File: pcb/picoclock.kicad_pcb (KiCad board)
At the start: 2 copper layers, 175.8 x 64 mm, 54 parts, among them J1 UART, J10 USB, J2 AUDIO, J3 xx, J4 xx, J5 Power In, J6 USB_C_Receptacle, J7 xx, J8 xx, J9 screen_adapter_connector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

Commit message: update case+pcb
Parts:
- added R10: 10K, Resistor_SMD:R_0603_1608Metric, B.Cu at (138.1, 109.4)
- added R11: 10K, Resistor_SMD:R_0603_1608Metric, B.Cu at (138.1, 113.2)
- added R12: 10K, Resistor_SMD:R_0603_1608Metric, B.Cu at (187.9, 112.7)
- added R13: 10K, Resistor_SMD:R_0603_1608Metric, B.Cu at (188.9, 98.5)
- added R8: 10K, Resistor_SMD:R_0603_1608Metric, B.Cu at (189.1, 82.0)
- added R9: 10K, Resistor_SMD:R_0603_1608Metric, B.Cu at (138.1, 106.4)
- H1, H2, H3, H4: footprint MountingHole:MountingHole_2.5mm -> MountingHole:MountingHole_3mm_Pad
- moved JP2 0.21 mm to (69.2, 103.2)
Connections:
- J4 pad 4: unconnected-(J4-Pin_4-Pad4) -> SDA
- J4 pad 5: unconnected-(J4-Pin_5-Pad5) -> SCL
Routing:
- net +3.3V: track 193.4 -> 244.2 mm
- net SDA: track 22.9 -> 72.5 mm, vias 2 -> 3
- net SCL: track 25.4 -> 74.4 mm, vias 0 -> 2
- net GPIO8: track 42.9 -> 45.3 mm
- net GPIO9: track 37.5 -> 39.5 mm

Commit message: [pcb] update
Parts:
- added BT1: 3V Cell, cell:MPD_BC501SM-TR, F.Cu at (214.9, 105.7)
- added J11: Alt Power, Connector_PinHeader_2.54mm:PinHeader_1x02_P2.54mm_Vertical, F.Cu at (171.1, 119.6)
- C1, C2, C3, C4, C5, C9: footprint Capacitor_SMD:C_0402_1005Metric -> Capacitor_SMD:C_0603_1608Metric
- R2, R4: footprint Resistor_SMD:R_0402_1005Metric -> Resistor_SMD:R_0603_1608Metric
- moved C2 14.2 mm to (173.6, 122.8), turned to 180 degrees
- moved R1 5.48 mm to (177.7, 116.8), turned to 0 degrees
- moved H6 5.05 mm to (172.3, 110.2)
- moved H8 5.05 mm to (230.3, 110.2)
- moved H5 5.05 mm to (172.3, 87.5)
- moved H7 5.05 mm to (230.3, 87.5)
- moved U1 2.23 mm to (178.9, 121.1)
- moved Y1 2.23 mm to (186.1, 120.0)
- moved R3 2.20 mm to (168.1, 116.2)
- moved C1 2.08 mm to (183.8, 118.4)
- moved U3 1.78 mm to (178.9, 113.6)
- moved R2 0.75 mm to (126.2, 121.3)
- moved C7 0.65 mm to (127.4, 123.3)
- moved C8 0.65 mm to (126.0, 123.3)
- moved C5 0.61 mm to (127.5, 125.4)
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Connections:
- C2 pad 1: +3.3V -> 3V BATT
- U1 pad 8: +3.3V -> 3V BATT
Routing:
- net 3V BATT: track 0.00 -> 57.9 mm, vias 0 -> 1
- net SDA: track 72.5 -> 78.1 mm, vias 3 -> 2
- net SQW: track 14.6 -> 19.2 mm
- net GPIO1 SCREEN RST: track 33.7 -> 36.8 mm
- net GPIO5 SCREEN BUSY: track 37.2 -> 39.8 mm
- net GPIO1 SCREEN CS: track 29.2 -> 27.5 mm
- net GPIO10: track 41.5 -> 42.5 mm
- net GND: track 20.4 -> 19.8 mm, vias 4 -> 5
- net SCL: track 74.4 -> 74.5 mm, vias 2 -> 4
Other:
- board text added: "+3.3V"
- board text added: "+5V"
- board text added: "AGND"
- board text added: "AUDIO_L"
- board text added: "AUDIO_R"
- board text added: "BUSY"
- board text added: "CS"
- board text added: "D+"
- board text added: "D-"
- board text added: "DATA"
- board text added: "GND"
- board text added: "GP11"
- board text added: "RST"
- board text added: "RX"
- board text added: "SCL"
- board text added: "SDA"
- board text added: "TX"

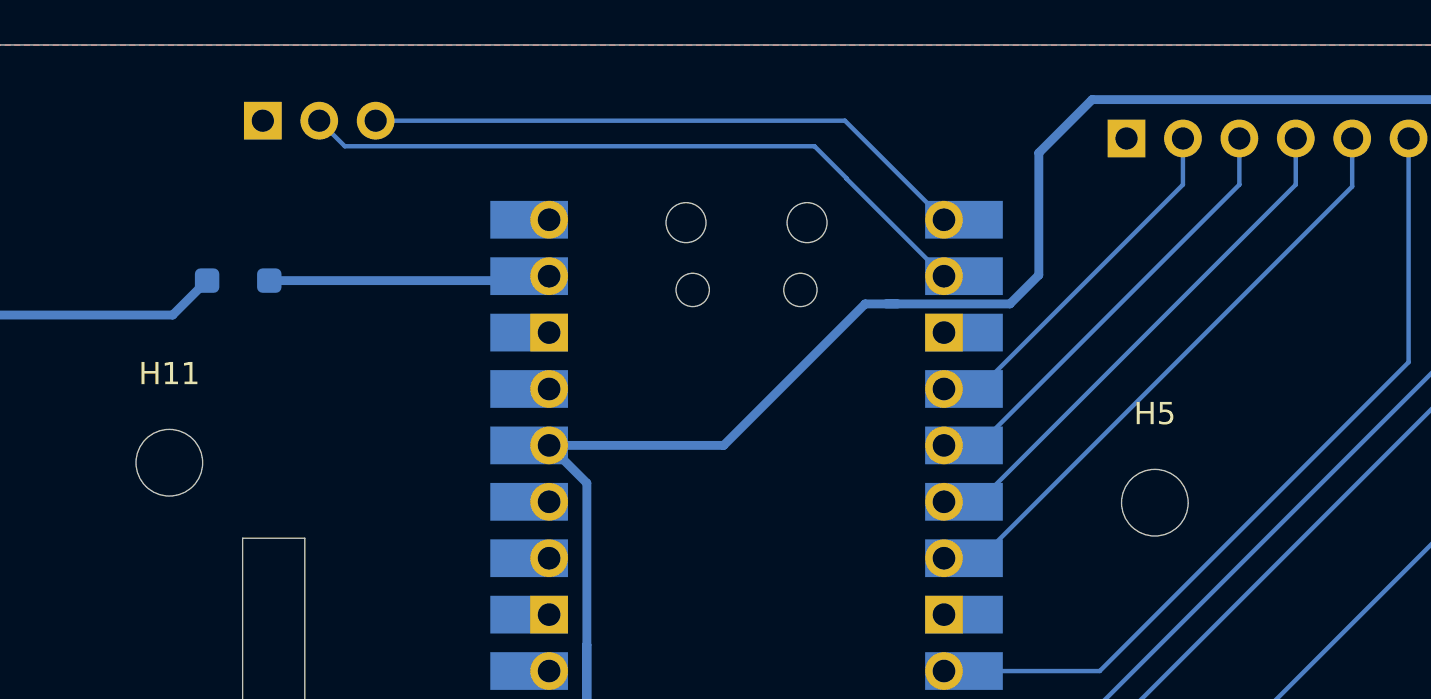
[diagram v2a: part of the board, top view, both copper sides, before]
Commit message: [pcb] fix epaper hat position, fix GPIO, add labels
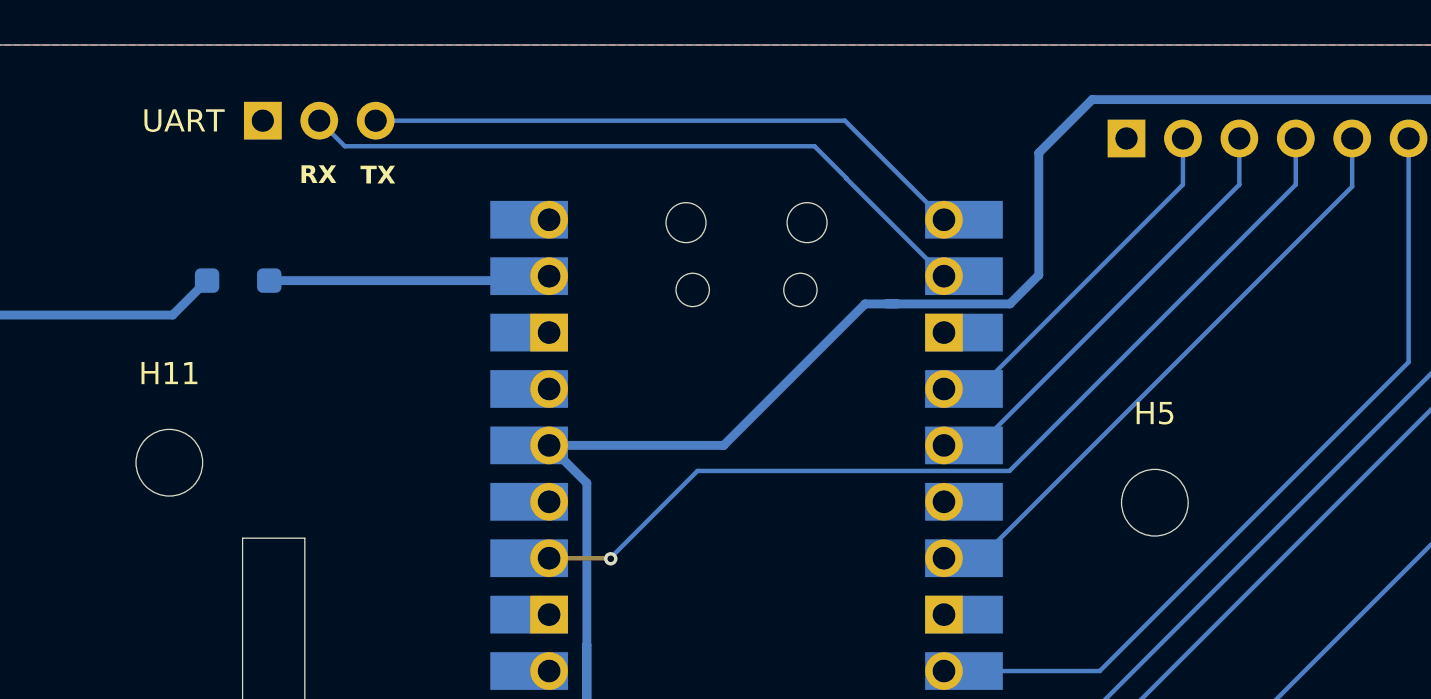
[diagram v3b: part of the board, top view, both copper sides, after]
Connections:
- net GPIO2 SCREEN DATA renamed GPIO2 CLK
- J9 pad 4: GPIO4 SPI0 RX -> GPIO28 DC
- U2 pad 34: unconnected-(U2-GPIO28_ADC2-Pad34) -> GPIO28 DC
- U2 pad 6: GPIO4 SPI0 RX -> unconnected-(U2-GPIO4-Pad6)
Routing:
- net GPIO28 DC: track 0.00 -> 42.8 mm, vias 0 -> 1
- net GPIO4 SPI0 RX: track 23.8 -> 0.00 mm
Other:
- board text added: "CLK"
- board text removed: "DATA"

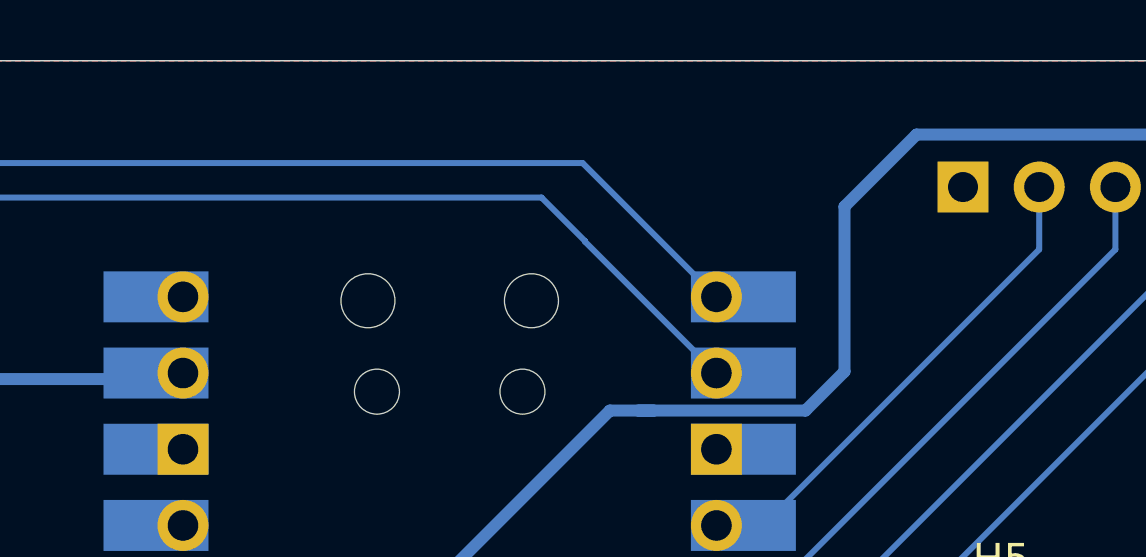
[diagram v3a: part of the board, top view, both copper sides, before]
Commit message: [pcb] add PWR from epaper hat
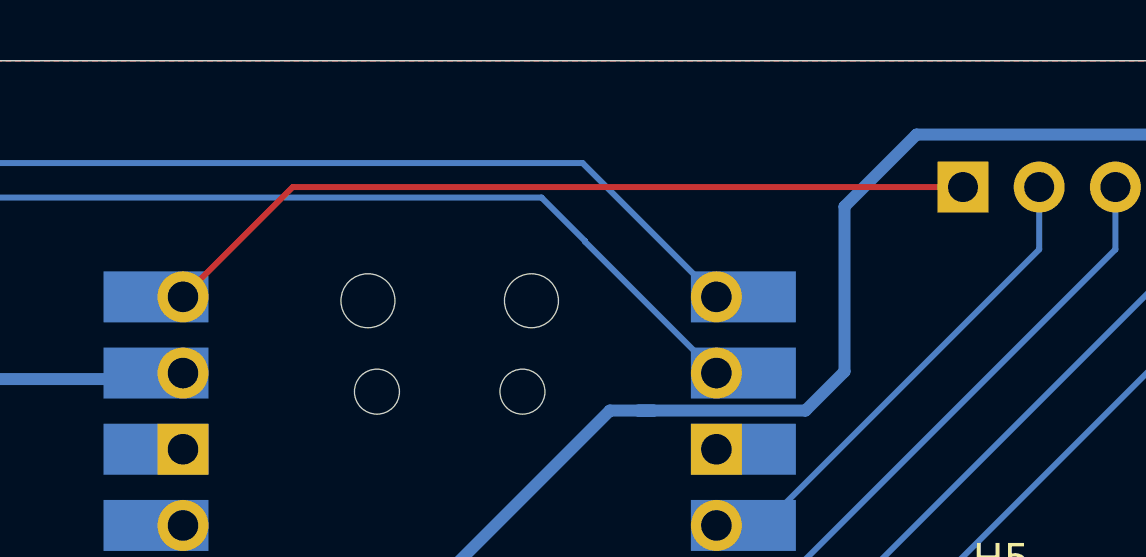
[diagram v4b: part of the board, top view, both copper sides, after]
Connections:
- J9 pad 1: unconnected-(J9-Pin_1-Pad1) -> PWR
- U2 pad 40: unconnected-(U2-VBUS-Pad40) -> PWR
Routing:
- net PWR: track 0.00 -> 27.5 mm

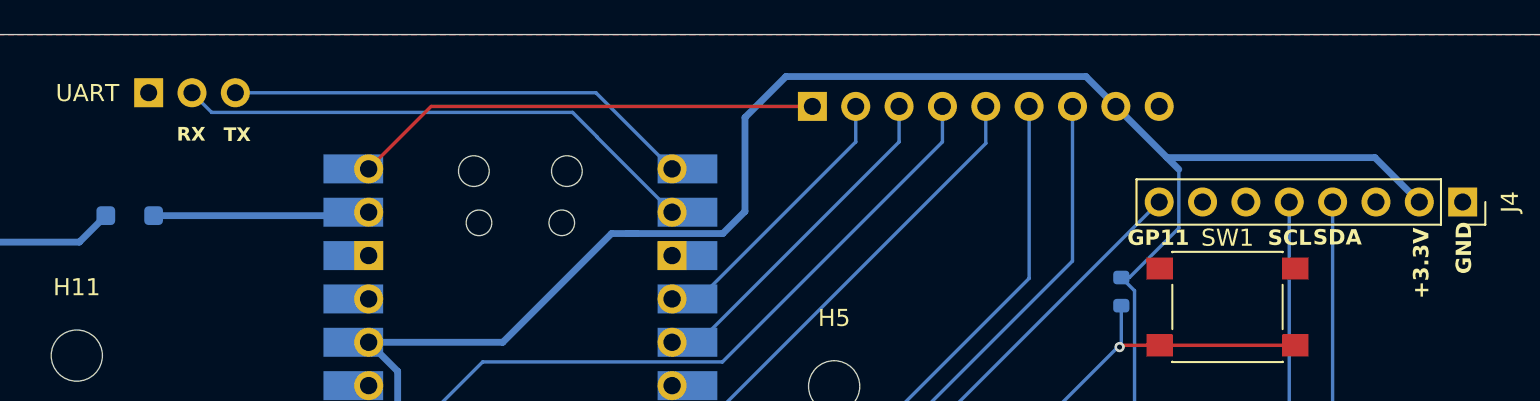
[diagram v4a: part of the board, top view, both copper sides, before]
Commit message: [pcb] fix frontpanel pcb LEDs + connexion to main pcb
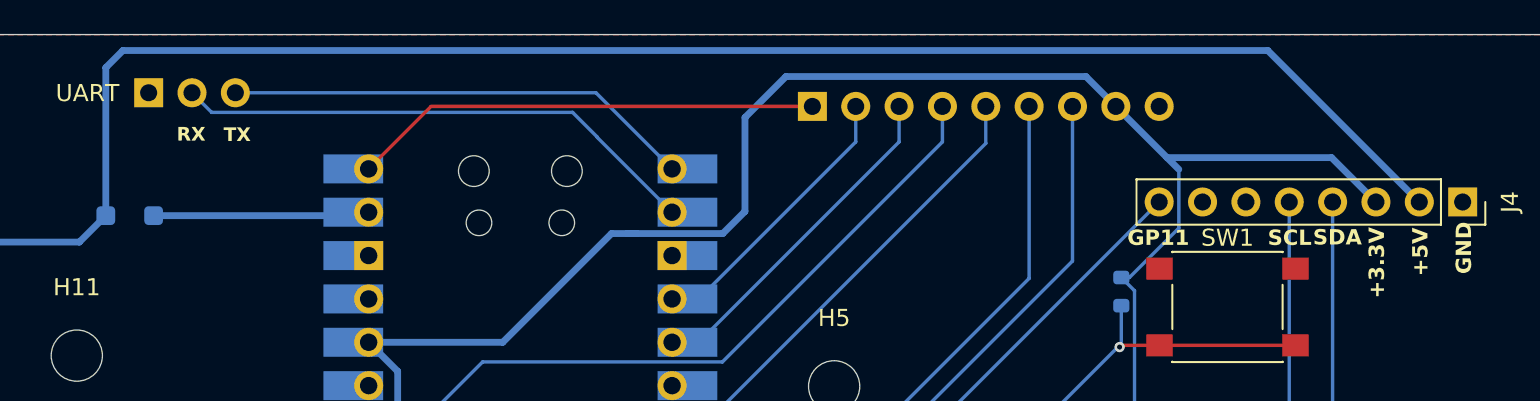
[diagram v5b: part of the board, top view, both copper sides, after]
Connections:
- J4 pad 2: +3.3V -> +5V
- J4 pad 3: unconnected-(J4-Pin_3-Pad3) -> +3.3V
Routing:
- net +5V: track 106.2 -> 195.9 mm
- net +3.3V: track 244.0 -> 241.5 mm

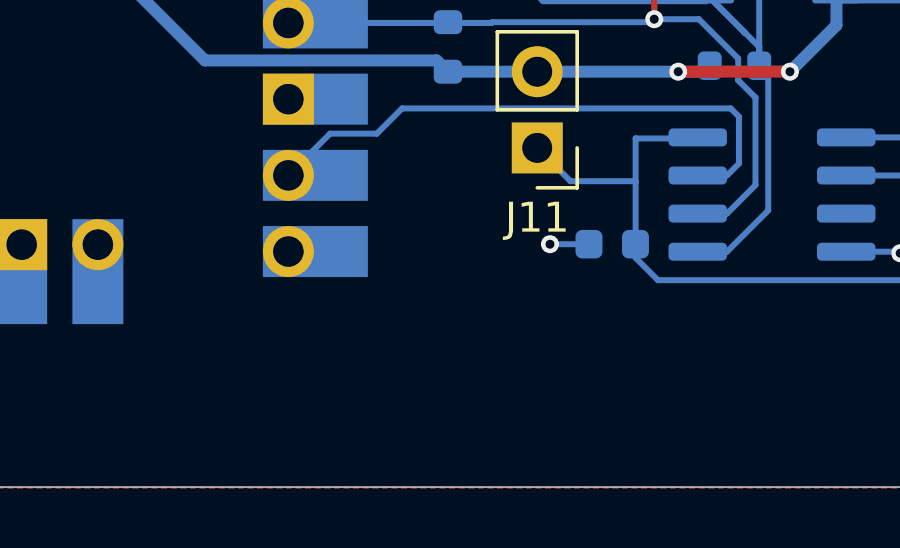
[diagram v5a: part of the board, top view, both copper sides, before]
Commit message: [pcb] add PWM out
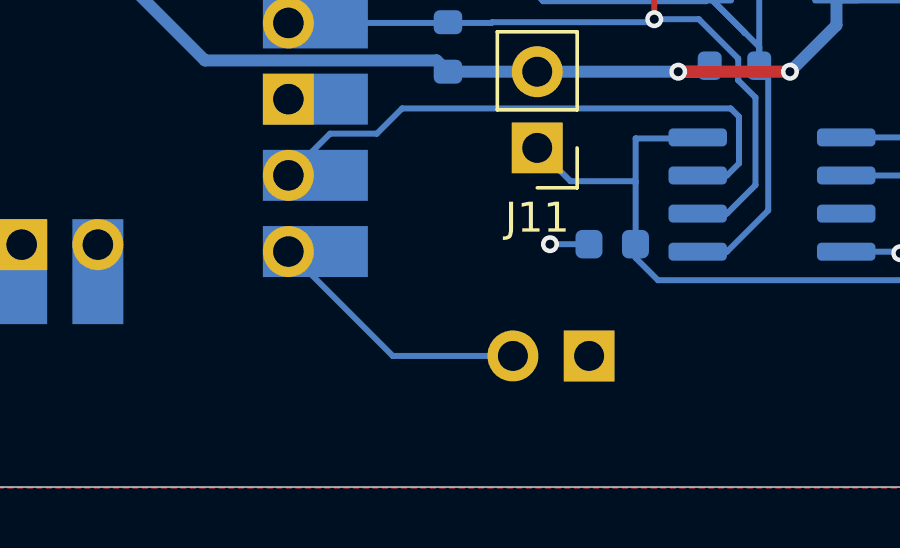
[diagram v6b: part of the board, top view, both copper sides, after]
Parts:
- added J12: PWM, Connector_PinHeader_2.54mm:PinHeader_1x02_P2.54mm_Vertical, B.Cu at (172.8, 126.5)
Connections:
- U2 pad 20: unconnected-(U2-GPIO15-Pad20) -> GPIO15 / PWM
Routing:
- net GPIO15 / PWM: track 0.00 -> 8.93 mm
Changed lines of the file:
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@@
   (net 23 "DIN")
   (net 24 "LRCK")
-  (net 25 "unconnected-(U2-GPIO15-Pad20)")
+  (net 25 "GPIO15 {slash} PWM")
   (net 26 "unconnected-(U2-RUN-Pad30)")
   (net 27 "unconnected-(U2-ADC_VREF-Pad35)")
@@
       (net 20 "SQW") (pinfunction "GPIO14") (pintype "bidirectional"))
     (pad "20" thru_hole oval (at -8.89 -24.13 180) (size 1.7 1.7) (drill 1.02) (layers "*.Cu" "*.Mask")
-      (net 25 "unconnected-(U2-GPIO15-Pad20)") (pinfunction "GPIO15") (pintype "bidirectional+no_connect"))
+      (net 25 "GPIO15 {slash} PWM") (pinfunction "GPIO15") (pintype "bidirectional"))
     (pad "20" smd rect (at -8.89 -24.13 180) (size 3.5 1.7) (drill (offset -0.9 0)) (layers "B.Cu" "B.Mask")
-      (net 25 "unconnected-(U2-GPIO15-Pad20)") (pinfunction "GPIO15") (pintype "bidirectional+no_connect"))
+      (net 25 "GPIO15 {slash} PWM") (pinfunction "GPIO15") (pintype "bidirectional"))
     (pad "21" thru_hole oval (at 8.89 -24.13 180) (size 1.7 1.7) (drill 1.02) (layers "*.Cu" "*.Mask")
       (net 23 "DIN") (pinfunction "GPIO16") (pintype "bidirectional"))
@@
     )
   )
+  (footprint "Connector_PinHeader_2.54mm:PinHeader_1x02_P2.54mm_Vertical" (layer "B.Cu")
+    (at 172.805 126.5 90)
+    (descr "Through hole straight pin header, 1x02, 2.54mm pitch, single row")
+    (tags "Through hole pin header THT 1x02 2.54mm single row")
+    (property "Sheetfile" "picoclock.kicad_sch")
+    (property "Sheetname" "")
+    (property "ki_description" "Generic connector, single row, 01x02, script generated")
+    (property "ki_keywords" "connector")
+    (attr through_hole)
+    (fp_text reference "J12" (at 0 2.33 90) (layer "B.SilkS")
+        (effects (font (size 1 1) (thickness 0.15)) (justify mirror))
+    )
+    (fp_text value "PWM" (at 0 -4.87 90) (layer "B.Fab")
+        (effects (font (size 1 1) (thickness 0.15)) (justify mirror))
+    )
+    (fp_text user "${REFERENCE}" (at 0 -1.27) (layer "B.Fab")
+        (effects (font (size 1 1) (thickness 0.15)) (justify mirror))
+    )
+    (fp_line (start -1.33 -3.87) (end 1.33 -3.87)
+      (stroke (width 0.12) (type solid)) (layer "B.SilkS"))
+    (fp_line (start -1.33 -1.27) (end -1.33 -3.87)
+      (stroke (width 0.12) (type solid)) (layer "B.SilkS"))
+    (fp_line (start -1.33 -1.27) (end 1.33 -1.27)
+      (stroke (width 0.12) (type solid)) (layer "B.SilkS"))
+    (fp_line (start -1.33 0) (end -1.33 1.33)
+      (stroke (width 0.12) (type solid)) (layer "B.SilkS"))
+    (fp_line (start -1.33 1.33) (end 0 1.33)
+      (stroke (width 0.12) (type solid)) (layer "B.SilkS"))
+    (fp_line (start 1.33 -1.27) (end 1.33 -3.87)
+      (stroke (width 0.12) (type solid)) (layer "B.SilkS"))
+    (fp_line (start -1.8 -4.35) (end 1.8 -4.35)
+      (stroke (width 0.05) (type solid)) (layer "B.CrtYd"))
+    (fp_line (start -1.8 1.8) (end -1.8 -4.35)
+      (stroke (width 0.05) (type solid)) (layer "B.CrtYd"))
+    (fp_line (start 1.8 -4.35) (end 1.8 1.8)
+      (stroke (width 0.05) (type solid)) (layer "B.CrtYd"))
+    (fp_line (start 1.8 1.8) (end -1.8 1.8)
+      (stroke (width 0.05) (type solid)) (layer "B.CrtYd"))
+    (fp_line (start -1.27 -3.81) (end -1.27 0.635)
+      (stroke (width 0.1) (type solid)) (layer "B.Fab"))
+    (fp_line (start -1.27 0.635) (end -0.635 1.27)
+      (stroke (width 0.1) (type solid)) (layer "B.Fab"))
+    (fp_line (start -0.635 1.27) (end 1.27 1.27)
+      (stroke (width 0.1) (type solid)) (layer "B.Fab"))
+    (fp_line (start 1.27 -3.81) (end -1.27 -3.81)
+      (stroke (width 0.1) (type solid)) (layer "B.Fab"))
+    (fp_line (start 1.27 1.27) (end 1.27 -3.81)
+      (stroke (width 0.1) (type solid)) (layer "B.Fab"))
+    (pad "1" thru_hole rect (at 0 0 90) (size 1.7 1.7) (drill 1) (layers "*.Cu" "*.Mask")
+      (net 1 "GND") (pinfunction "Pin_1") (pintype "passive"))
+    (pad "2" thru_hole oval (at 0 -2.54 90) (size 1.7 1.7) (drill 1) (layers "*.Cu" "*.Mask")
+      (net 25 "GPIO15 {slash} PWM") (pinfunction "Pin_2") (pintype "passive"))
+    (model "${KICAD6_3DMODEL_DIR}/Connector_PinHeader_2.54mm.3dshapes/PinHeader_1x02_P2.54mm_Vertical.wrl"
+      (offset (xyz 0 0 0))
+      (scale (xyz 1 1 1))
+      (rotate (xyz 0 0 0))
+    )
+  )
   (footprint "Resistor_SMD:R_0603_1608Metric" (layer "B.Cu")
     (at 177.65 116.825)
@@
   (segment (start 146.2 116.6) (end 145 115.4) (width 0.2) (layer "B.Cu") (net 24))
   (segment (start 135.8 121.65) (end 139.98 121.65) (width 0.2) (layer "B.Cu") (net 24))
+  (segment (start 166.26 126.5) (end 170.265 126.5) (width 0.2) (layer "B.Cu") (net 25))
+  (segment (start 162.78 123.02) (end 166.26 126.5) (width 0.2) (layer "B.Cu") (net 25))
   (segment (start 148.66 71.1) (end 145 74.76) (width 0.2) (layer "F.Cu") (net 29))
   (segment (start 171 71.1) (end 148.66 71.1) (width 0.2) (layer "F.Cu") (net 29))
